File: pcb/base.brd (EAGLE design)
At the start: 78 x 78 mm, 21 parts, among them IC1 TINY24/44/84-PU, J1 22-27-2051-05, J2 22-27-2051-05, J3 22-27-2051-05, J4 22-27-2051-05, J5 22-27-2051-05, J6 22-27-2021-02

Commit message: add voltage regulator and other clamp
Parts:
- removed J6: 22-27-2021-02, con-molex:6410-02
- added C2: (no value), rcl:E2,5-7
- added C3: (no value), rcl:C025-025X050
- added IC2: TS2940CT5TV, n39:TO220V
- added U$9: RIACON_101_2, n39:RIACON_101_2
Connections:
- new net N$4: IC2.1, U$9.2
- new net N$6: C3.1, U$9.1
- net GND: now also C2.-, C3.2, IC2.2; no longer J6.1
- net VCC: now also C2.+, IC2.3; no longer J6.2
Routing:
- net VCC: track 230.6 -> 218.6 mm
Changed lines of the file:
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@@
 <layer number="21" name="tPlace" color="7" fill="1" visible="yes" active="yes"/>
 <layer number="22" name="bPlace" color="7" fill="1" visible="yes" active="yes"/>
-<layer number="23" name="tOrigins" color="15" fill="1" visible="no" active="yes"/>
-<layer number="24" name="bOrigins" color="15" fill="1" visible="no" active="yes"/>
+<layer number="23" name="tOrigins" color="15" fill="1" visible="yes" active="yes"/>
+<layer number="24" name="bOrigins" color="15" fill="1" visible="yes" active="yes"/>
 <layer number="25" name="tNames" color="7" fill="1" visible="no" active="yes"/>
 <layer number="26" name="bNames" color="7" fill="1" visible="no" active="yes"/>
@@
 <param name="mtCopper" value="0.035mm 0.035mm 0.035mm 0.035mm 0.035mm 0.035mm 0.035mm 0.035mm 0.035mm 0.035mm 0.035mm 0.035mm 0.035mm 0.035mm 0.035mm 0.035mm"/>
 <param name="mtIsolate" value="1.5mm 0.15mm 0.2mm 0.15mm 0.2mm 0.15mm 0.2mm 0.15mm 0.2mm 0.15mm 0.2mm 0.15mm 0.2mm 0.15mm 0.2mm"/>
-<param name="mdWireWire" value="12mil"/>
-<param name="mdWirePad" value="12mil"/>
-<param name="mdWireVia" value="12mil"/>
-<param name="mdPadPad" value="12mil"/>
-<param name="mdPadVia" value="12mil"/>
-<param name="mdViaVia" value="12mil"/>
+<param name="mdWireWire" value="10mil"/>
+<param name="mdWirePad" value="10mil"/>
+<param name="mdWireVia" value="10mil"/>
+<param name="mdPadPad" value="10mil"/>
+<param name="mdPadVia" value="10mil"/>
+<param name="mdViaVia" value="10mil"/>
 <param name="mdSmdPad" value="8mil"/>
 <param name="mdSmdVia" value="8mil"/>
@@
 <param name="mdSmdStop" value="0mil"/>
 <param name="msWidth" value="12mil"/>
-<param name="msDrill" value="0.6mm"/>
+<param name="msDrill" value="0.8mm"/>
 <param name="msMicroVia" value="9.99mm"/>
 <param name="msBlindViaRatio" value="0.5"/>
-<param name="rvPadTop" value="0.25"/>
-<param name="rvPadInner" value="0.25"/>
-<param name="rvPadBottom" value="0.25"/>
-<param name="rvViaOuter" value="0.25"/>
-<param name="rvViaInner" value="0.25"/>
+<param name="rvPadTop" value="0.3"/>
+<param name="rvPadInner" value="0.3"/>
+<param name="rvPadBottom" value="0.3"/>
+<param name="rvViaOuter" value="0.3"/>
+<param name="rvViaInner" value="0.3"/>
 <param name="rvMicroViaOuter" value="0.25"/>
 <param name="rvMicroViaInner" value="0.25"/>
@@
 <element name="R3" library="pot" package="CIP20C-6MM" value="100k" x="74" y="39" rot="R90"/>
 <element name="R4" library="pot" package="CIP20C-6MM" value="100k" x="39" y="74" rot="R180"/>
-<element name="J6" library="con-molex" package="6410-02" value="22-27-2021-02" x="66.04" y="12.065" rot="R180">
-<attribute name="OC_NEWARK" value="unknown" x="66.04" y="12.065" size="1.778" layer="27" rot="R180" display="off"/>
-<attribute name="MPN" value="" x="66.04" y="12.065" size="1.778" layer="27" rot="R180" display="off"/>
-<attribute name="MF" value="" x="66.04" y="12.065" size="1.778" layer="27" rot="R180" display="off"/>
-<attribute name="OC_FARNELL" value="unknown" x="66.04" y="12.065" size="1.778" layer="27" rot="R180" display="off"/>
-</element>
+<element name="U$9" library="n39" package="RIACON_101_2" value="RIACON_101_2" x="-55.88" y="6.35">
+<attribute name="REICHELT" value="AKL 101-02" x="-55.88" y="6.35" size="1.778" layer="27" display="off"/>
+</element>
+<element name="IC2" library="n39" package="TO220V" value="TS2940CT5TV" x="-54.61" y="-1.27">
+<attribute name="REICHELT" value="LM 2940 CT5" x="-54.61" y="-1.27" size="1.778" layer="27" display="off"/>
+</element>
+<element name="C2" library="rcl" package="E2,5-7" value="" x="-57.15" y="-13.97"/>
+<element name="C3" library="rcl" package="C025-025X050" value="" x="-57.15" y="-21.59"/>
 </elements>
 <signals>
@@
 <contactref element="J3" pad="1"/>
 <contactref element="J4" pad="1"/>
-<contactref element="J6" pad="2"/>
 <wire x1="3.175" y1="64.77" x2="3.175" y2="66.04" width="0.8128" layer="16"/>
 <wire x1="3.175" y1="66.04" x2="6.985" y2="69.85" width="0.8128" layer="16"/>
@@
 <wire x1="74.93" y1="33.07" x2="74" y2="34" width="0.8128" layer="16"/>
 <wire x1="74.93" y1="21.59" x2="74.93" y2="19.685" width="0.8128" layer="16"/>
-<wire x1="74.93" y1="19.685" x2="67.31" y2="12.065" width="0.8128" layer="16"/>
-<wire x1="67.31" y1="12.065" x2="67.31" y2="10.795" width="0.8128" layer="16"/>
 <wire x1="67.31" y1="10.795" x2="62.865" y2="6.35" width="0.8128" layer="16"/>
 <wire x1="62.865" y1="6.35" x2="48.895" y2="6.35" width="0.8128" layer="16"/>
@@
 <wire x1="3.175" y1="44.825" x2="4" y2="44" width="0.8128" layer="16"/>
 <wire x1="3.175" y1="55.245" x2="3.175" y2="64.77" width="0.8128" layer="16"/>
+<contactref element="IC2" pad="3"/>
+<contactref element="C2" pad="+"/>
+<wire x1="-52.07" y1="-3.81" x2="-58.42" y2="-13.97" width="0" layer="19" extent="1-1"/>
+<wire x1="1.27" y1="15.24" x2="-52.07" y2="-3.81" width="0" layer="19" extent="16-16"/>
+<wire x1="67.31" y1="10.795" x2="74.93" y2="19.685" width="0" layer="19" extent="16-16"/>
 </signal>
 <signal name="GND" class="1">
@@
 <via x="15.24" y="60.325" extent="1-16" drill="0.8" shape="square"/>
 <wire x1="5.715" y1="60.325" x2="15.24" y2="60.325" width="0.8128" layer="1"/>
-<contactref element="J6" pad="1"/>
+<contactref element="IC2" pad="2"/>
+<contactref element="IC2" pad="2"/>
+<contactref element="C3" pad="2"/>
+<contactref element="C2" pad="-"/>
+<wire x1="73.025" y1="55.245" x2="73.025" y2="64.77" width="0" layer="19" extent="1-1"/>
+<wire x1="62.23" y1="64.77" x2="73.025" y2="64.77" width="0" layer="19" extent="1-1"/>
+<wire x1="74" y1="44" x2="73.025" y2="55.245" width="0" layer="19" extent="1-1"/>
+<wire x1="72.39" y1="21.59" x2="74" y2="44" width="0" layer="19" extent="1-1"/>
+<wire x1="34" y1="74" x2="62.23" y2="71.755" width="0" layer="19" extent="1-1"/>
+<wire x1="15.24" y1="60.325" x2="34" y2="74" width="0" layer="19" extent="1-1"/>
+<wire x1="5.715" y1="64.77" x2="5.715" y2="60.325" width="0" layer="19" extent="1-1"/>
+<wire x1="5.715" y1="55.245" x2="5.715" y2="60.325" width="0" layer="19" extent="1-1"/>
+<wire x1="4" y1="34" x2="5.715" y2="55.245" width="0" layer="19" extent="1-1"/>
+<wire x1="10.795" y1="11.43" x2="4" y2="34" width="0" layer="19" extent="1-1"/>
+<wire x1="10.795" y1="8.57" x2="10.795" y2="11.43" width="0" layer="19" extent="16-16"/>
+<wire x1="43.815" y1="6.35" x2="72.39" y2="21.59" width="0" layer="19" extent="1-1"/>
+<wire x1="-54.61" y1="-3.81" x2="10.795" y2="8.57" width="0" layer="19" extent="16-16"/>
+<wire x1="-55.88" y1="-13.97" x2="-54.61" y2="-3.81" width="0" layer="19" extent="1-1"/>
+<wire x1="-55.88" y1="-21.59" x2="-55.88" y2="-13.97" width="0" layer="19" extent="1-1"/>
 </signal>
 <signal name="MISO" class="2">
@@
 <wire x1="18.415" y1="13.97" x2="12.065" y2="20.32" width="0.3048" layer="16"/>
 </signal>
+<signal name="N$4">
+<contactref element="U$9" pad="2"/>
+<contactref element="IC2" pad="1"/>
+<wire x1="-53.34" y1="6.35" x2="-57.15" y2="-3.81" width="0" layer="19" extent="1-1"/>
+</signal>
+<signal name="N$6">
+<contactref element="U$9" pad="1"/>
+<contactref element="C3" pad="1"/>
+<wire x1="-58.42" y1="6.35" x2="-58.42" y2="-21.59" width="0" layer="19" extent="1-1"/>
+</signal>
 </signals>

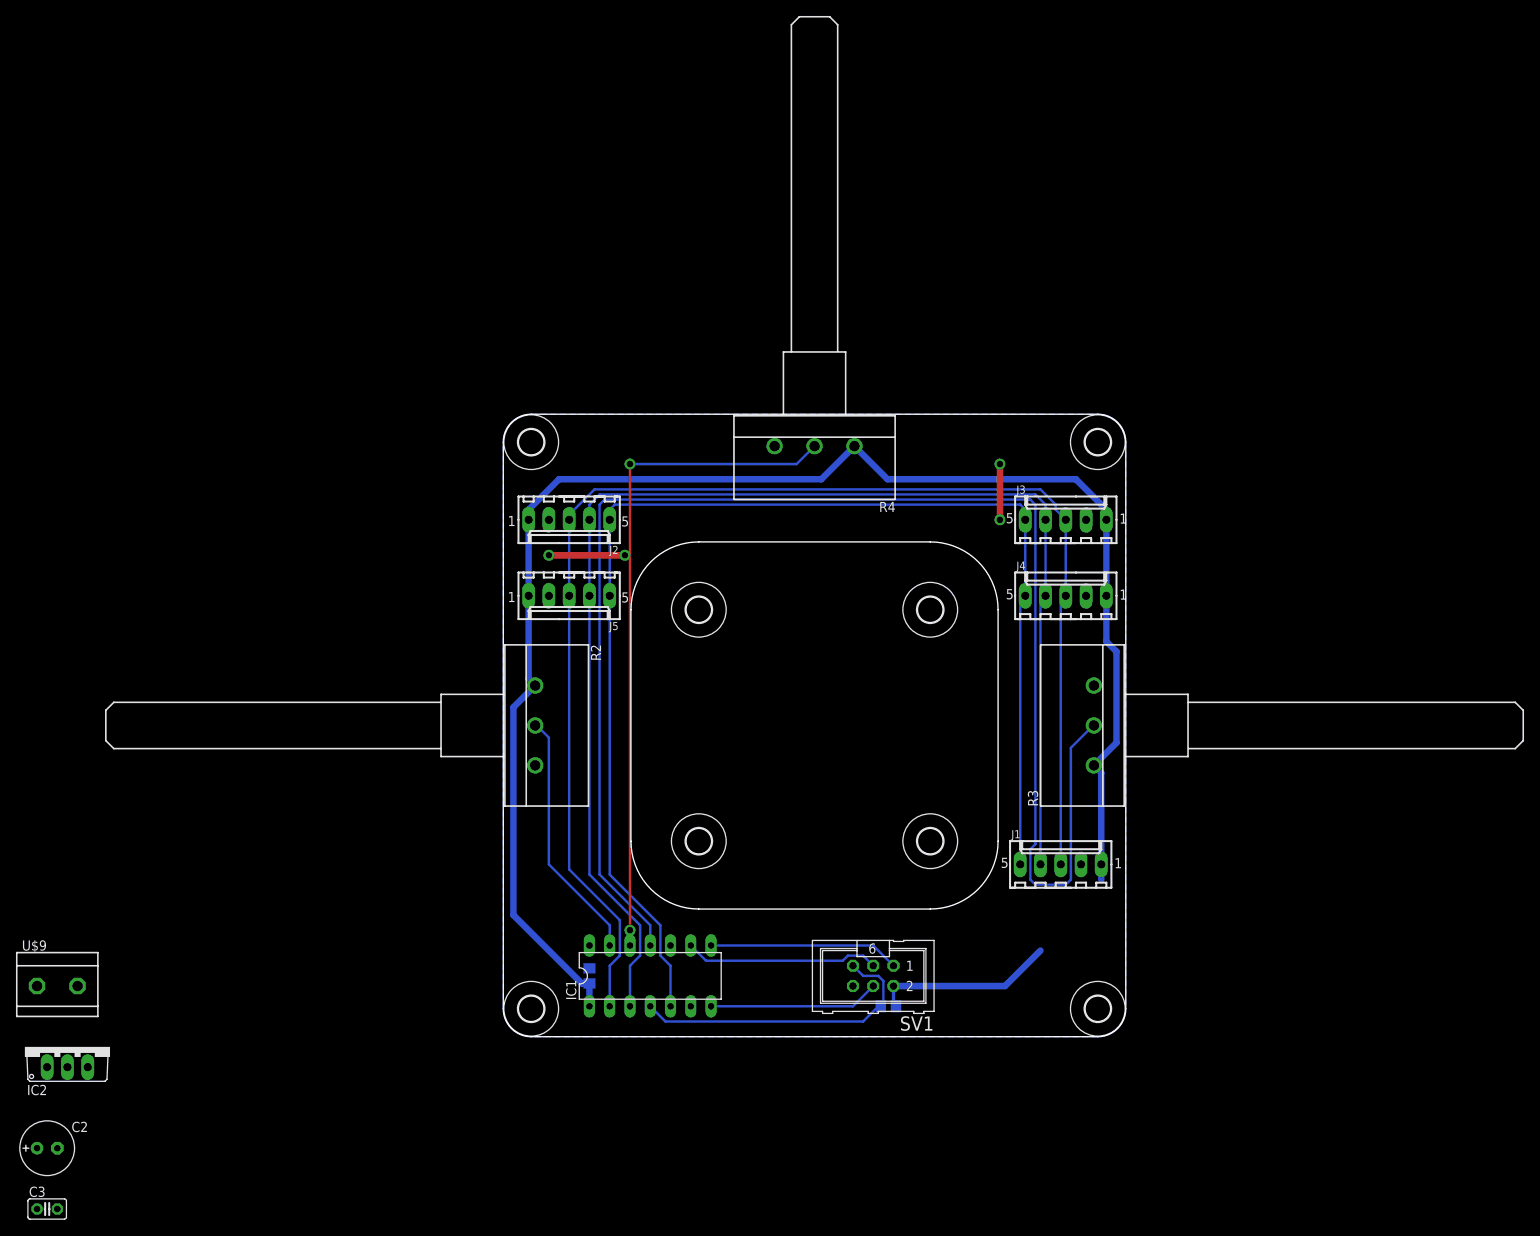
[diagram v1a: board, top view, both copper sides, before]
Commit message: route voltage regulator
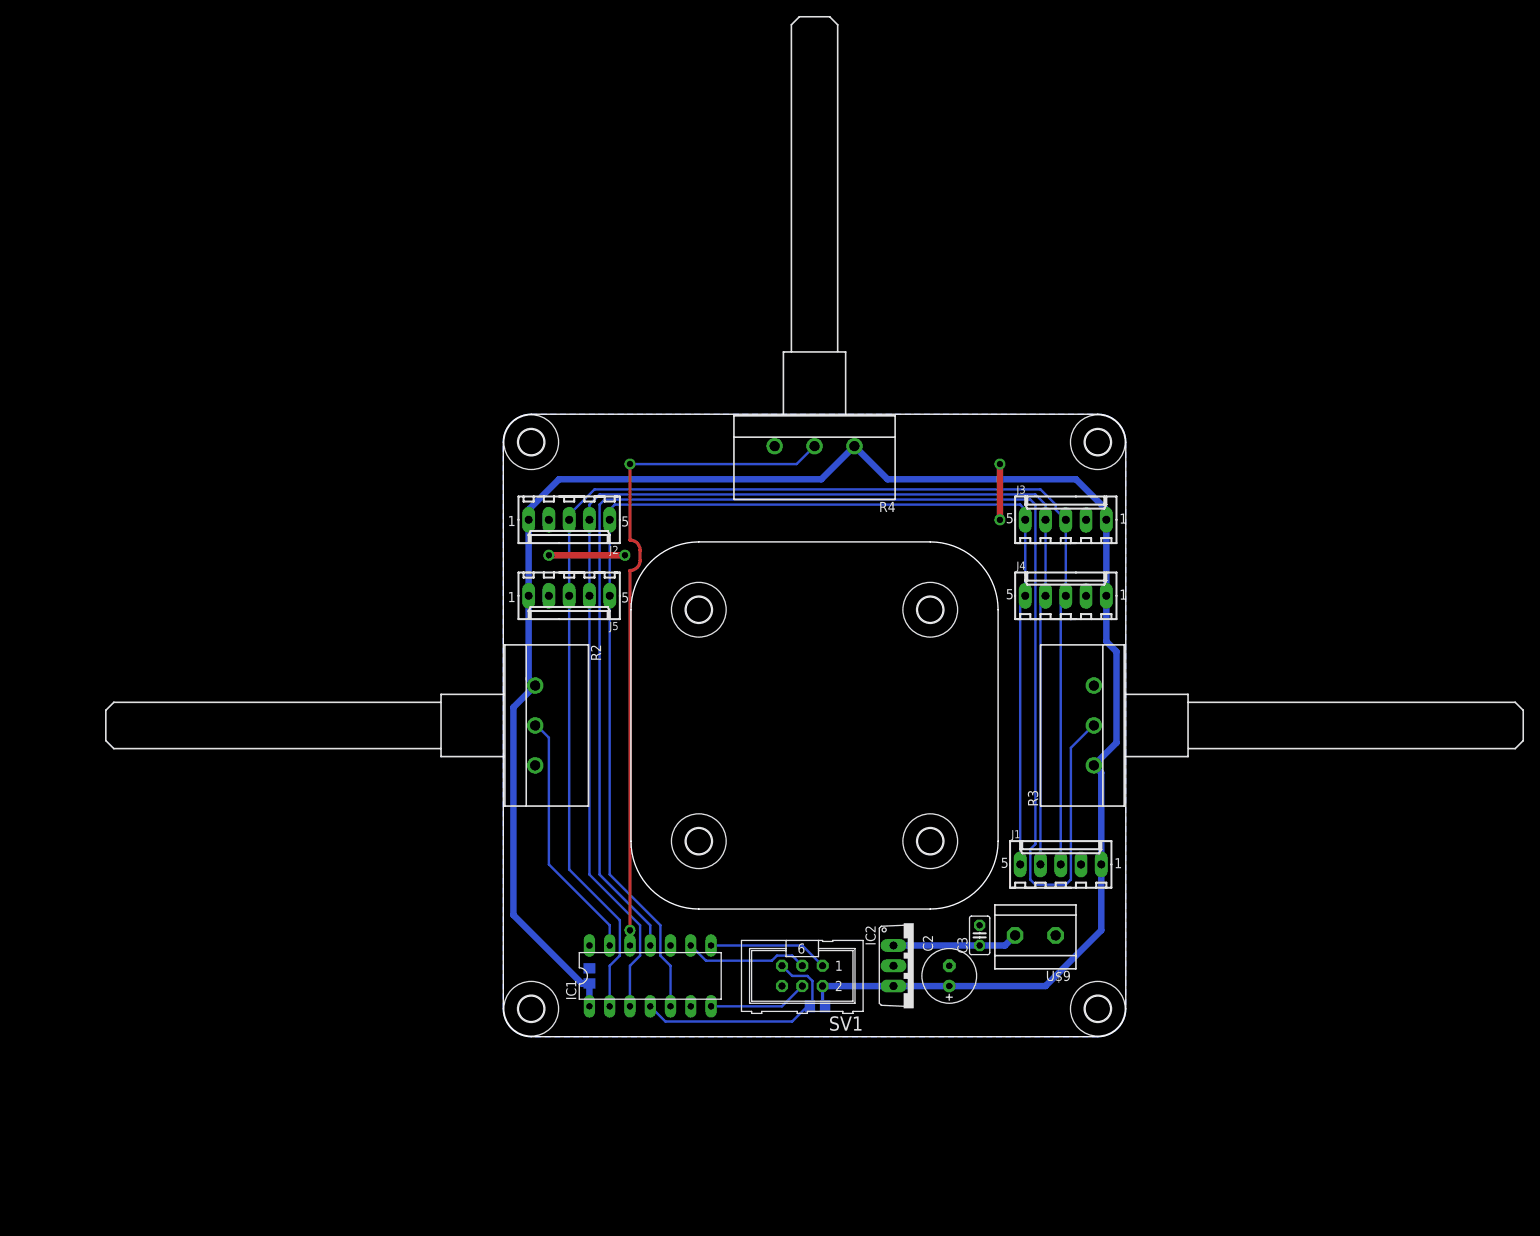
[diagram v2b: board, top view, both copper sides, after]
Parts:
- moved U$9 122.7 mm to (66.7, 12.7), turned to 180 degrees
- moved C3 121.8 mm to (59.7, 12.7), turned to 90 degrees
- moved C2 115.1 mm to (55.9, 7.62), turned to 90 degrees
- moved IC2 106.5 mm to (51.4, 8.89), turned to 270 degrees
- moved R1 8.89 mm to (39.4, 3.81)
- moved SV1 8.89 mm to (37.5, 7.62)
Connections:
- removed net N$6: C3.1, U$9.1
- net GND: now also U$9.1
- net N$4: now also C3.1
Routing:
- net VCC: track 218.6 -> 242.5 mm
- net N$4: track 0.00 -> 15.8 mm
- net MISO: track 23.9 -> 15.0 mm
- net !RESET: track 38.6 -> 29.7 mm
- net MOSI: track 21.4 -> 12.5 mm
- net SCK: track 24.4 -> 15.5 mm
- net N$2: track 84.4 -> 85.4 mm
